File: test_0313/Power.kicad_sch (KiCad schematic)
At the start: 3 parts, among them J5 USB_B_Mini, U1 ATmega16U2-M

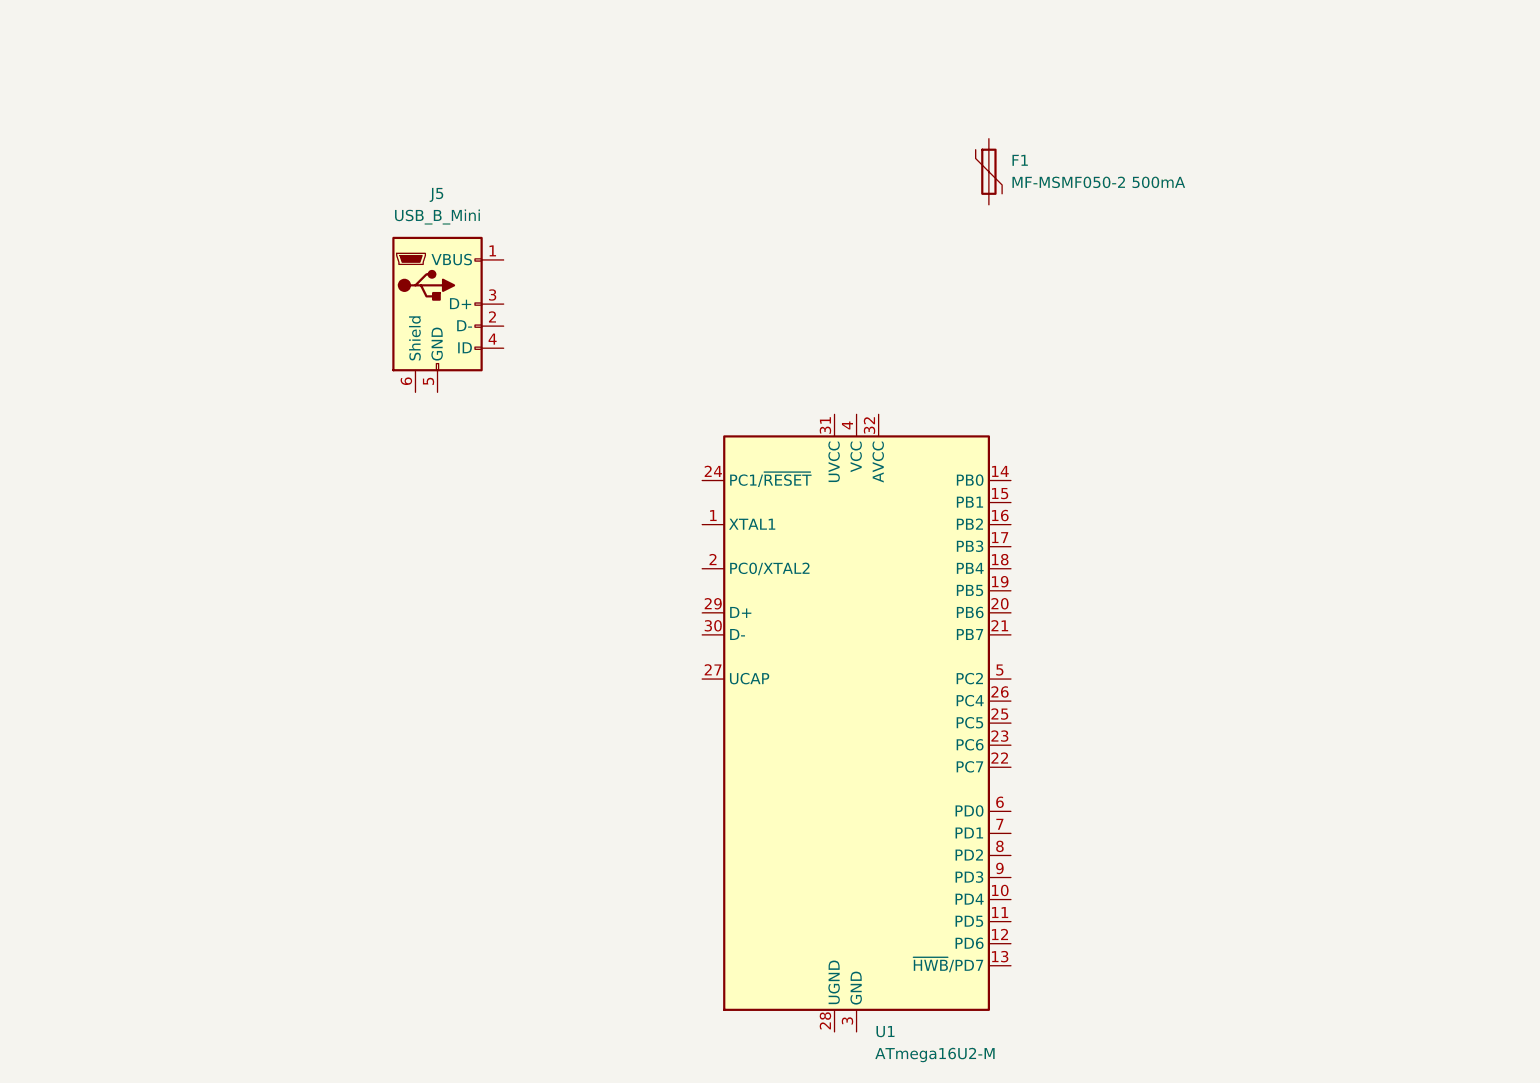
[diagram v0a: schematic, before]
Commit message: Update Power.kicad_sch
放置Power元件
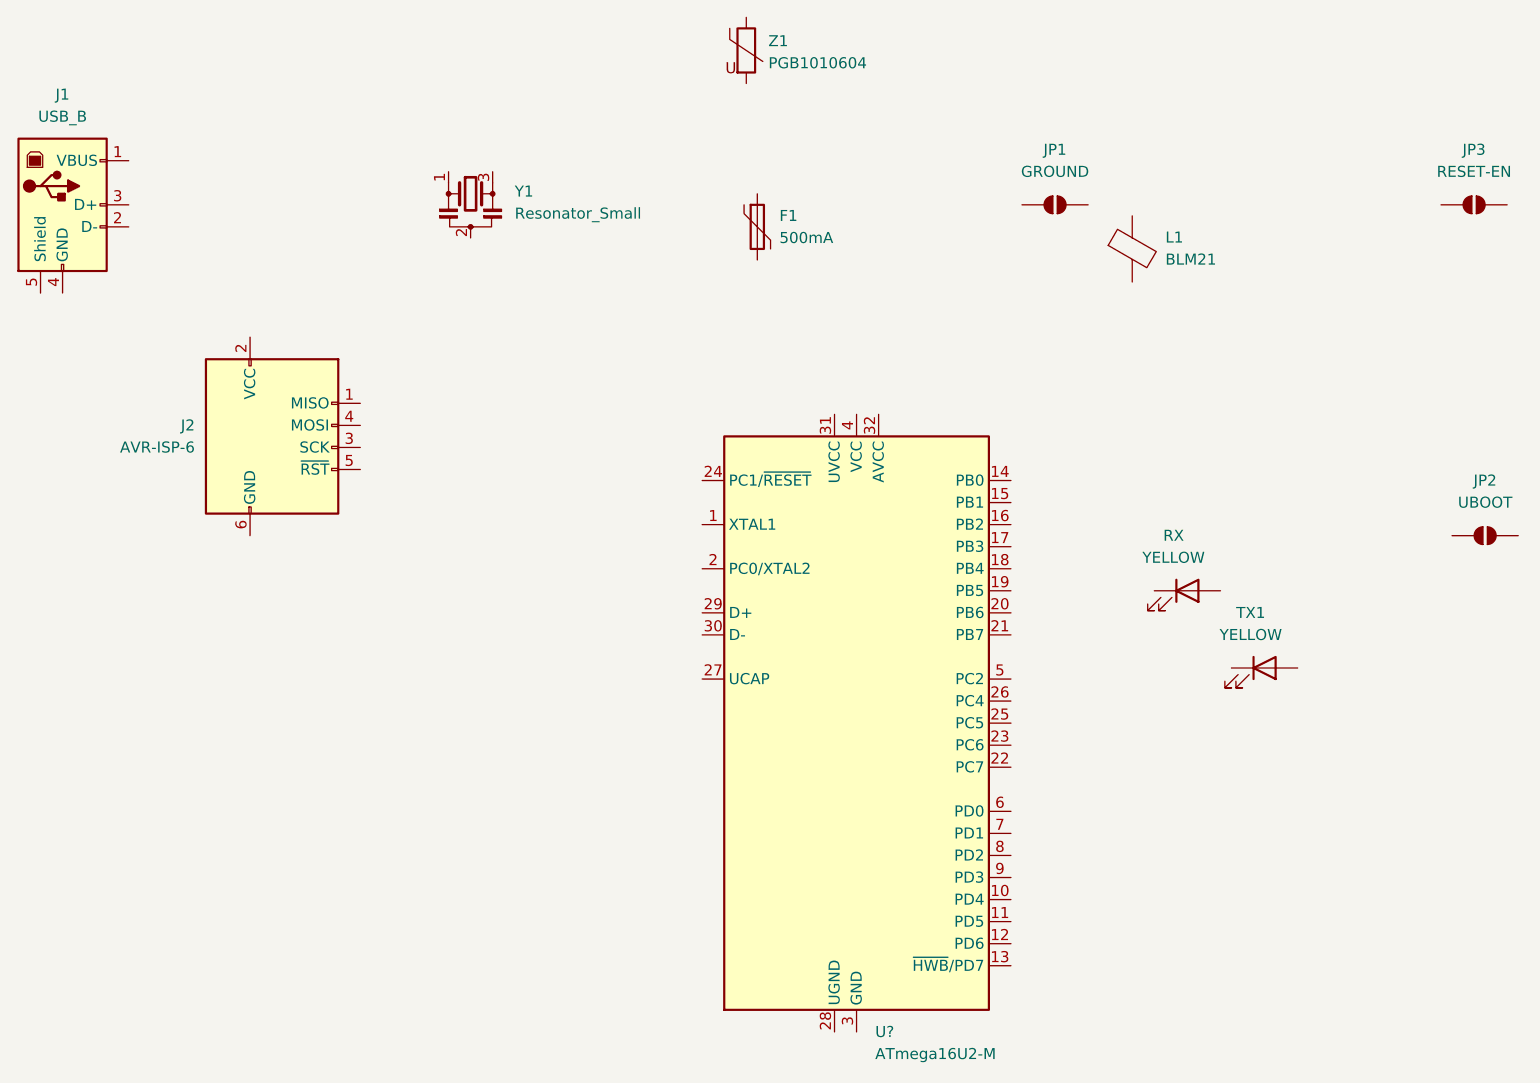
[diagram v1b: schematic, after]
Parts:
- removed J5: USB_B_Mini, Connector_USB:USB_Mini-B_Lumberg_2486_01_Horizontal, symbol Connector:USB_B_Mini
- added J1: USB_B, Connector_USB:USB_B_OST_USB-B1HSxx_Horizontal, symbol Connector:USB_B
- added J2: AVR-ISP-6, Connector_PinHeader_2.54mm:PinHeader_2x03_P2.54mm_Vertical, symbol Connector:AVR-ISP-6
- added JP1: GROUND, Jumper:SolderJumper-2_P1.3mm_Open_RoundedPad1.0x1.5mm, symbol Jumper:SolderJumper_2_Open
- added JP2: UBOOT, Jumper:SolderJumper-2_P1.3mm_Open_RoundedPad1.0x1.5mm, symbol Jumper:SolderJumper_2_Open
- added JP3: RESET-EN, Jumper:SolderJumper-2_P1.3mm_Open_RoundedPad1.0x1.5mm, symbol Jumper:SolderJumper_2_Open
- added L1: BLM21, Inductor_SMD:L_0805_2012Metric_Pad1.05x1.20mm_HandSolder, symbol Device:FerriteBead
- added RX, TX1: YELLOW, LED_SMD:LED_0603_1608Metric, symbol Device:LED
- added Y1: Resonator_Small, Crystal:Resonator_SMD_Murata_CSTxExxV-3Pin_3.0x1.1mm_HandSoldering, symbol Device:Resonator_Small
- added Z1: PGB1010604, Resistor_SMD:R_0603_1608Metric_Pad0.98x0.95mm_HandSolder, symbol Device:Varistor
- F1: value MF-MSMF050-2 500mA -> 500mA; footprint Fuse:Fuse_1206_3216Metric -> Fuse:Fuse_1812_4532Metric_Pad1.30x3.40mm_HandSolder
- renumbered U1 to U?

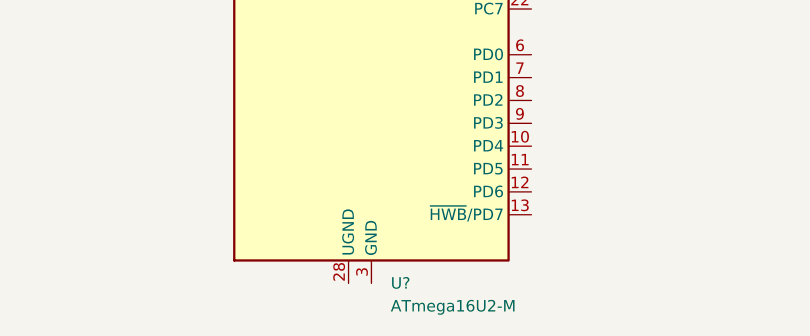
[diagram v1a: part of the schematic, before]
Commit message: 主原理圖當按位置錯誤修正
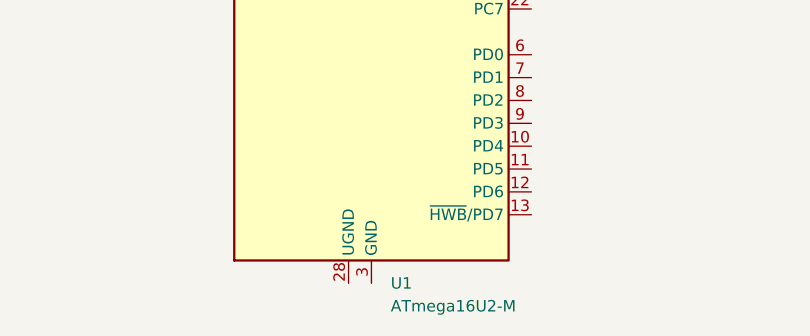
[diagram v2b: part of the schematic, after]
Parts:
- gave numbers to parts that had none: 1
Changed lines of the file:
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@@
+				)
+			)
+			(project ""
+				(path "/a3735c8f-9a58-4251-a332-2d5e31730472/11f5ab98-a620-47d0-8261-53f59b2985c2"
+					(reference "J2")
+					(unit 1)
 				)
 			)
@@
 				)
 			)
+			(project ""
+				(path "/a3735c8f-9a58-4251-a332-2d5e31730472/11f5ab98-a620-47d0-8261-53f59b2985c2"
+					(reference "Z1")
+					(unit 1)
+				)
+			)
 		)
 	)
@@
 				)
 			)
+			(project ""
+				(path "/a3735c8f-9a58-4251-a332-2d5e31730472/11f5ab98-a620-47d0-8261-53f59b2985c2"
+					(reference "F1")
+					(unit 1)
+				)
+			)
 		)
 	)
@@
 				)
 			)
+			(project ""
+				(path "/a3735c8f-9a58-4251-a332-2d5e31730472/11f5ab98-a620-47d0-8261-53f59b2985c2"
+					(reference "Y1")
+					(unit 1)
+				)
+			)
 		)
 	)
@@
 				)
 			)
+			(project ""
+				(path "/a3735c8f-9a58-4251-a332-2d5e31730472/11f5ab98-a620-47d0-8261-53f59b2985c2"
+					(reference "RX")
+					(unit 1)
+				)
+			)
 		)
 	)
@@
 				)
 			)
+			(project ""
+				(path "/a3735c8f-9a58-4251-a332-2d5e31730472/11f5ab98-a620-47d0-8261-53f59b2985c2"
+					(reference "L1")
+					(unit 1)
+				)
+			)
 		)
 	)
@@
 		(dnp no)
 		(fields_autoplaced yes)
-		(property "Reference" "U?"
+		(property "Reference" "U1"
 			(at 242.1733 200.66 0)
 			(effects
@@
 				)
 			)
-			(project ""
+			(project "Main"
 				(path "/a3735c8f-9a58-4251-a332-2d5e31730472/11f5ab98-a620-47d0-8261-53f59b2985c2"
 					(reference "U1")
@@
 				)
 			)
+			(project ""
+				(path "/a3735c8f-9a58-4251-a332-2d5e31730472/11f5ab98-a620-47d0-8261-53f59b2985c2"
+					(reference "J1")
+					(unit 1)
+				)
+			)
 		)
 	)
@@
 				)
 			)
+			(project ""
+				(path "/a3735c8f-9a58-4251-a332-2d5e31730472/11f5ab98-a620-47d0-8261-53f59b2985c2"
+					(reference "JP1")
+					(unit 1)
+				)
+			)
 		)
 	)
@@
 				)
 			)
+			(project "Power"
+				(path "/a3735c8f-9a58-4251-a332-2d5e31730472/11f5ab98-a620-47d0-8261-53f59b2985c2"
+					(reference "JP3")
+					(unit 1)
+				)
+			)
 		)
 	)
@@
 				)
 			)
+			(project ""
+				(path "/a3735c8f-9a58-4251-a332-2d5e31730472/11f5ab98-a620-47d0-8261-53f59b2985c2"
+					(reference "JP2")
+					(unit 1)
+				)
+			)
 		)
 	)
@@
 				)
 			)
-		)
-	)
-	(sheet_instances
-		(path "/"
-			(page "1")
-		)
-	)
-	(embedded_fonts no)
+			(project "Power"
+				(path "/a3735c8f-9a58-4251-a332-2d5e31730472/11f5ab98-a620-47d0-8261-53f59b2985c2"
+					(reference "TX1")
+					(unit 1)
+				)
+			)
+		)
+	)
 )
